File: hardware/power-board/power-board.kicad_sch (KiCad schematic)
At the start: 18 parts, among them J1 SW_SPST, J2 Conn_01x04, K1 SPST-NO, K2 SPST-NO, P1 IEC320-C14, P2 IEC320-C13, P3 IEC320-C13, U1 NUD3112DMT1G

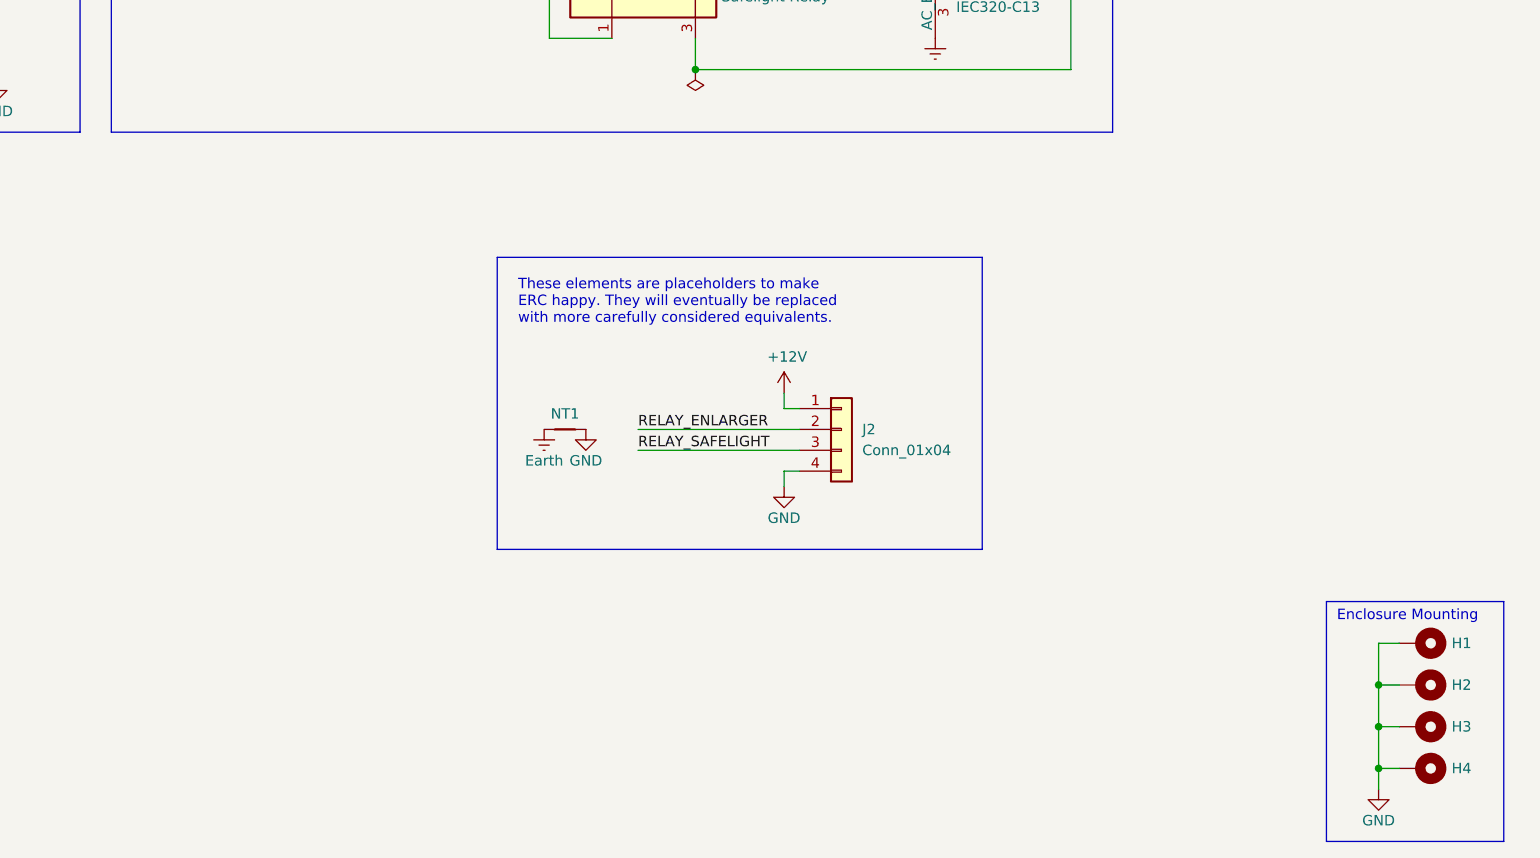
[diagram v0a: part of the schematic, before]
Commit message: WIP of adding XLR5 jack and making mechanical adjustments
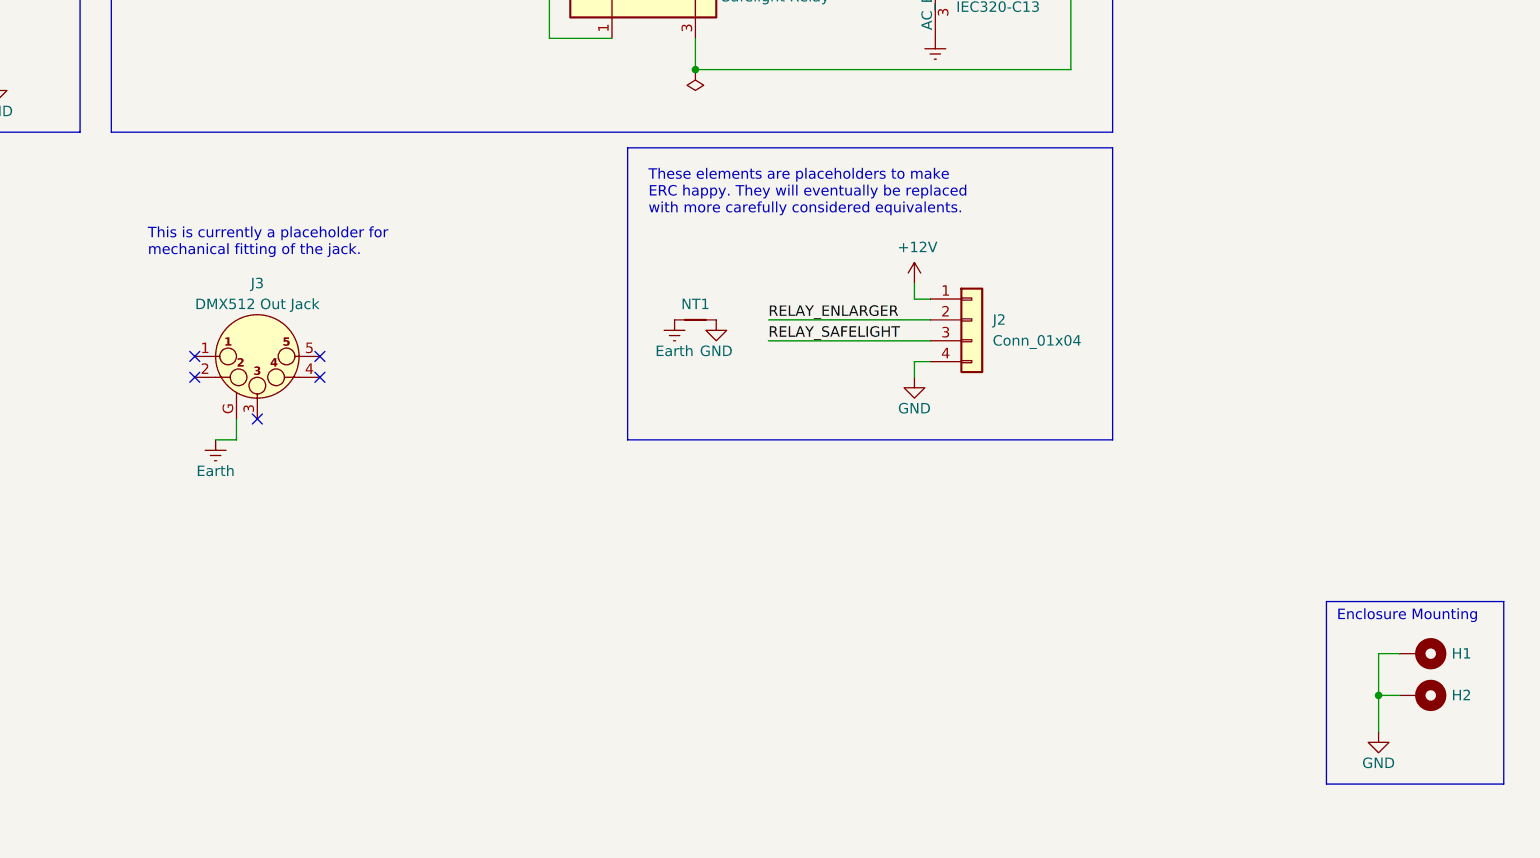
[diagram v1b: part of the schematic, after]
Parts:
- removed H3, H4: MountingHole_Pad, MountingHole:MountingHole_3.2mm_M3_Pad_Via, symbol Mechanical:MountingHole_Pad
- added J3: DMX512 Out Jack, Connector_Audio:Jack_XLR_Neutrik_NC5FBH_Horizontal, symbol Project:XLR5_Ground
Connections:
- net Earth: now also J3.G
- no-connect marks 0 -> 5
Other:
- note added: "This is currently a placeholder for mechanical fitting of the jack."
- moved on the sheet: H1, H2, J2, NT1

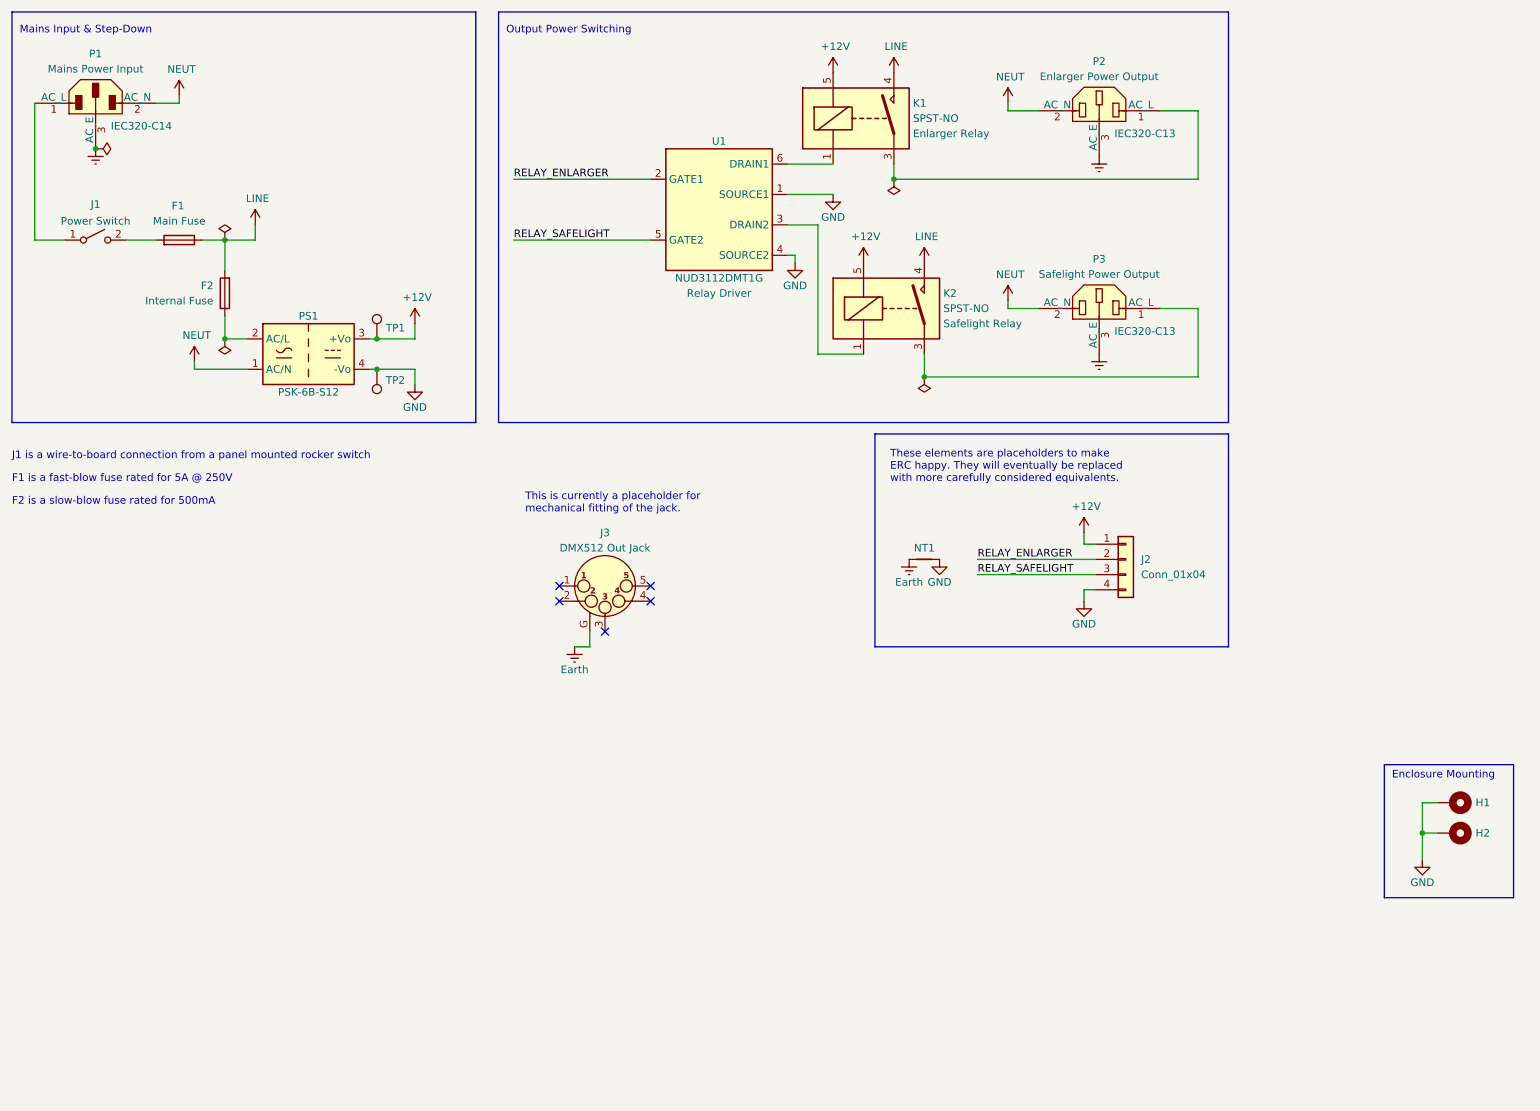
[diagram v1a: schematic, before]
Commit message: Initial addition of RS-485 interface components for DMX512
So far this is just getting the line driver on the board, in addition to
a few support components. Passives and internal connectors are still
placeholders.

The DMX512 spec says the transmitter should be earth referenced, not
isolated, so that helps make our driver and connector decisions.
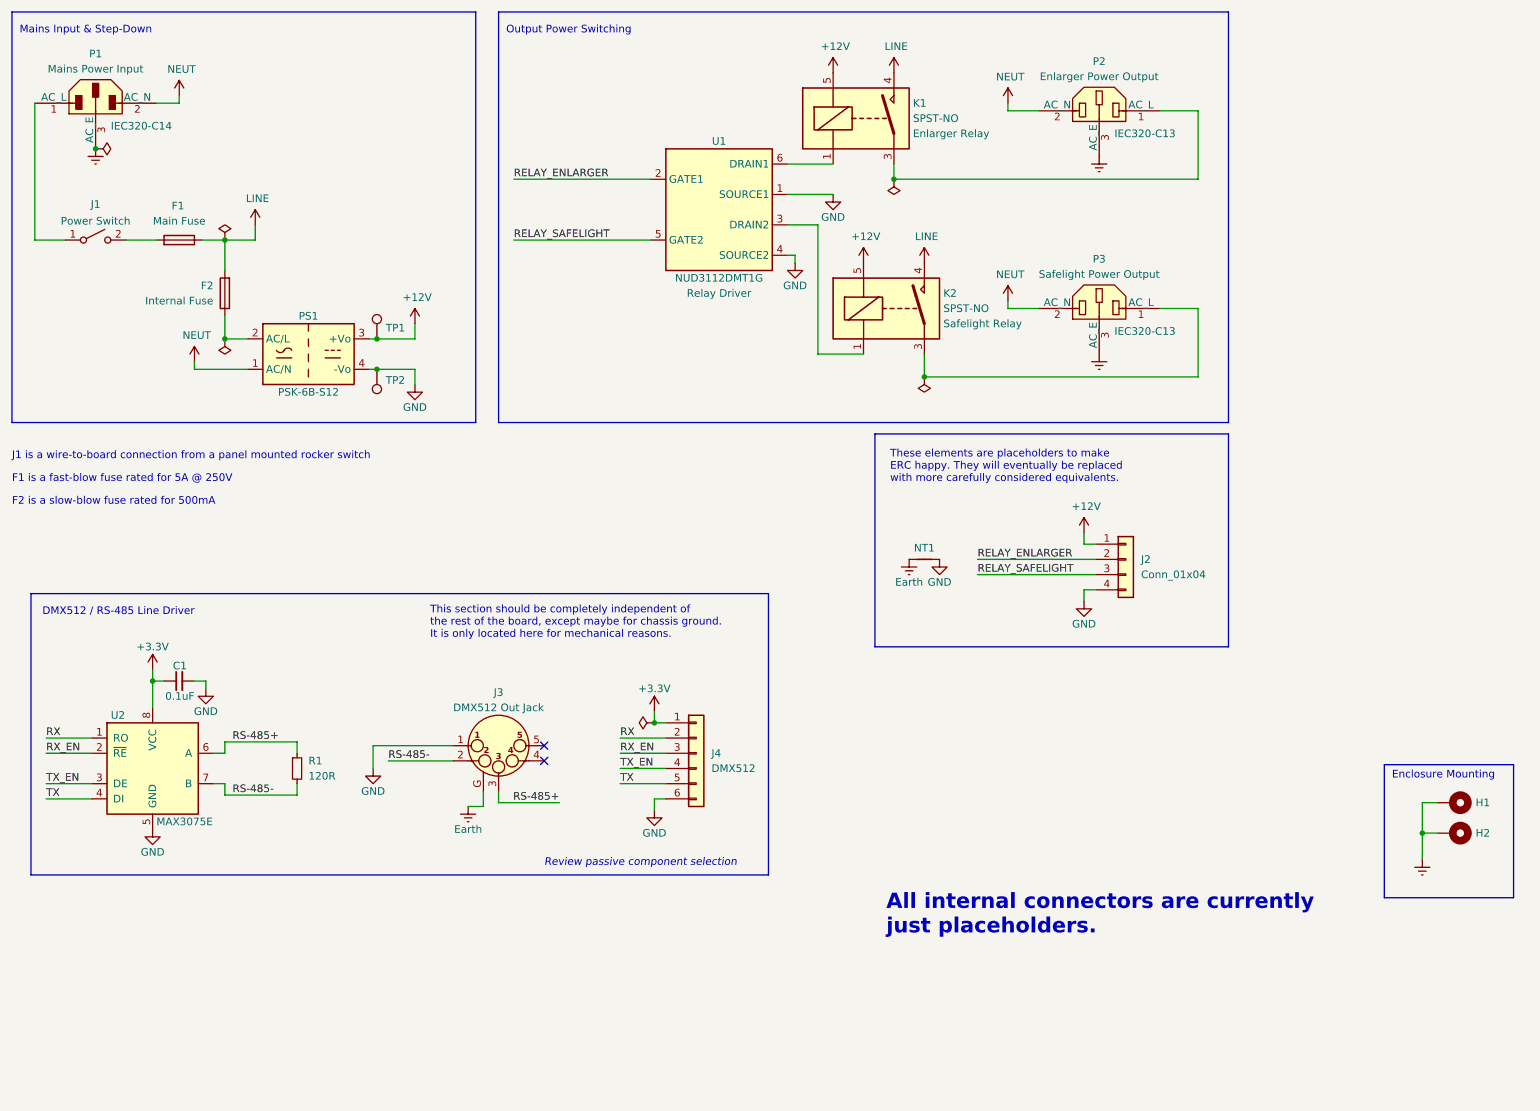
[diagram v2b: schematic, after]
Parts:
- added C1: 0.1uF, Capacitor_SMD:C_0805_2012Metric, symbol Device:C_Small
- added J4: DMX512, Connector_JST:JST_EH_B6B-EH-A_1x06_P2.50mm_Vertical, symbol Connector_Generic:Conn_01x06
- added R1: 120R, Resistor_SMD:R_0805_2012Metric, symbol Device:R_Small
- added U2: MAX3075E, Package_SO:SOIC-8_3.9x4.9mm_P1.27mm, symbol Interface_UART:MAX3075E
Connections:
- net Earth: now also H1.1, H2.1
- net GND: now also J3.1 (P1), C1.2, J4.6 (Pin_6), U2.5 (GND); no longer H1.1, H2.1
- net RS-485-: now reaches J3.2 (P2)
- net RS-485-: now also R1.2, U2.7 (B)
- net RS-485+: now reaches J3.3 (P3)
- net RS-485+: now also R1.1, U2.6 (A)
- new net +3.3V: C1.1, J4.1 (Pin_1), U2.8 (VCC)
- new net RX: J4.2 (Pin_2), U2.1 (RO)
- new net RX_EN: J4.3 (Pin_3), U2.2 (~{RE})
- new net TX: J4.5 (Pin_5), U2.4 (DI)
- new net TX_EN: J4.4 (Pin_4), U2.3 (DE)
- no-connect marks 5 -> 2
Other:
- note added: "All internal connectors are currently just placeholders."
- note added: "DMX512 / RS-485 Line Driver"
- note added: "Review passive component selection"
- note added: "This section should be completely independent of the rest of the board, except maybe for chassis ground. It is only located here for mechanical reasons."
- note removed: "This is currently a placeholder for mechanical fitting of the jack."
- moved on the sheet: J3

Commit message: Initial work on straightening out the AC/DC conversion components
Just some schematic and part selection work for now, to get a few extra
parts in place.
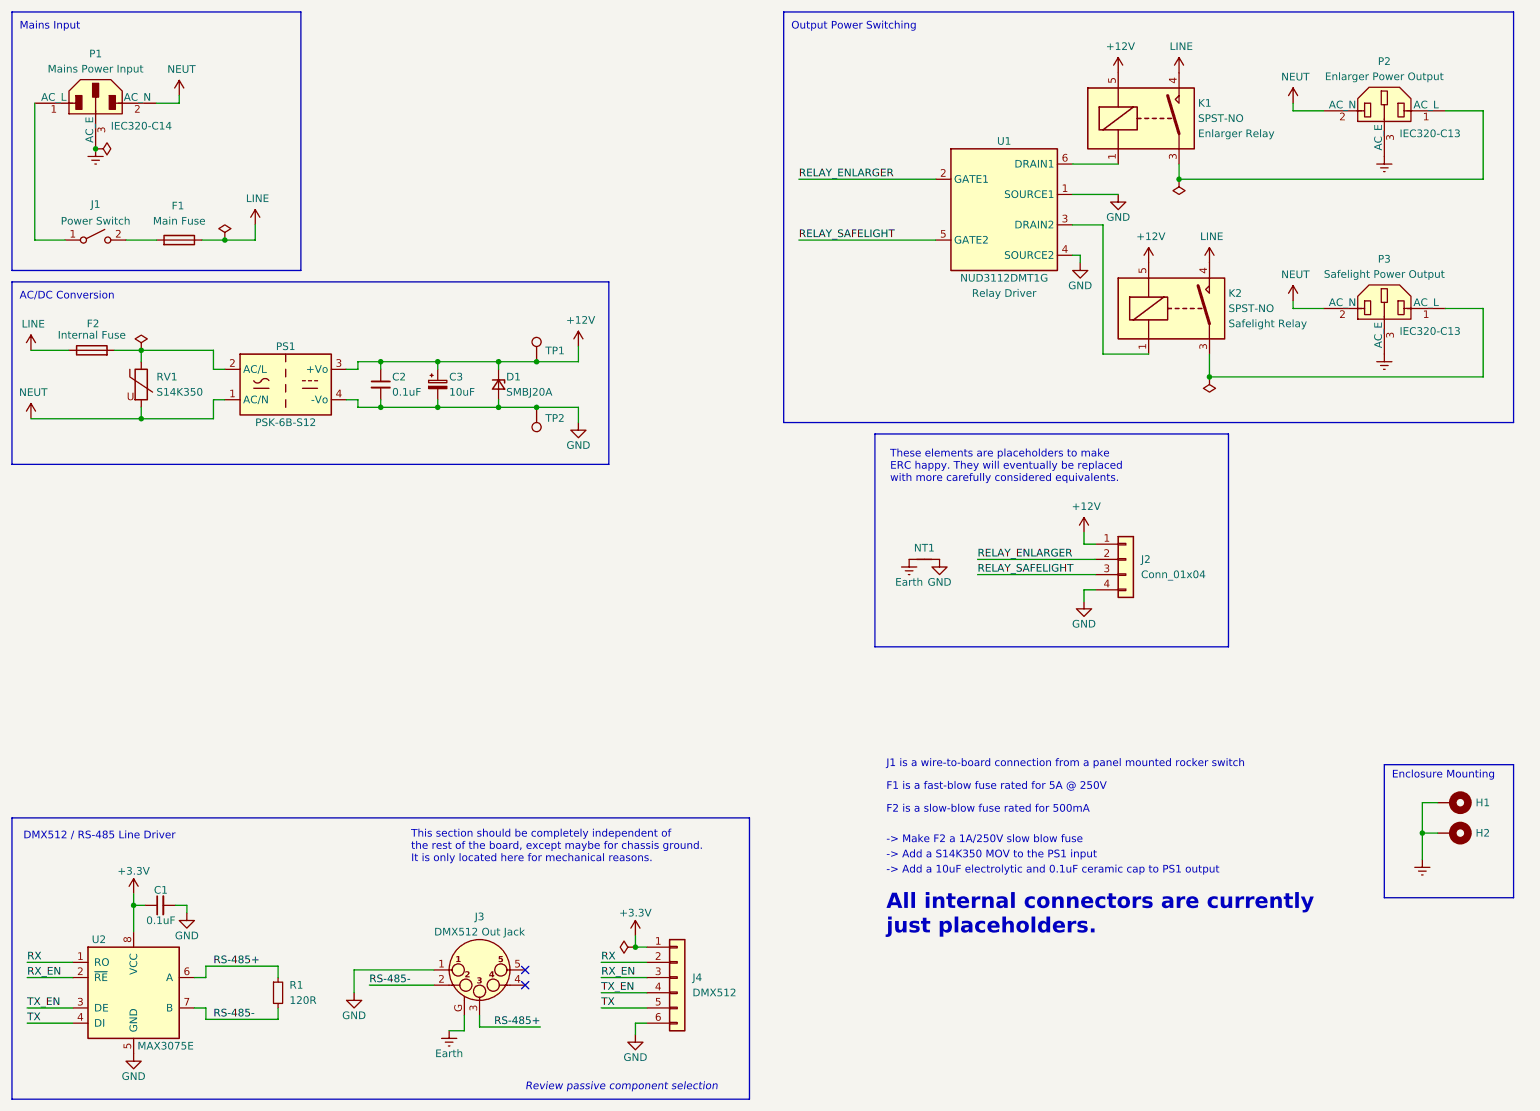
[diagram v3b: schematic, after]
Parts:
- added C2: 0.1uF, Capacitor_SMD:C_1206_3216Metric, symbol Device:C_Small
- added C3: 10uF, Capacitor_SMD:CP_Elec_6.3x5.4, symbol Device:C_Polarized_Small
- added D1: SMBJ20A, Diode_SMD:D_SMB, symbol Device:D_Zener_Small
- added RV1: S14K350, Varistor:RV_Disc_D15.5mm_W5.2mm_P7.5mm, symbol Device:Varistor
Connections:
- net +12V: now also C2.1, C3.1, D1.1 (K)
- net GND: now also C2.2, C3.2, D1.2 (A)
- net LINE: now also F2.1; no longer F2.2
- net NEUT: now also RV1.2
- net at PS1.2 (AC/L): now also F2.2, RV1.1; no longer F2.1
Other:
- note added: "-> Add a 10uF electrolytic and 0.1uF ceramic cap to PS1 output"
- note added: "-> Add a S14K350 MOV to the PS1 input"
- note added: "-> Make F2 a 1A/250V slow blow fuse"
- note added: "AC/DC Conversion"
- note added: "Mains Input"
- note removed: "Mains Input & Step-Down"
- moved on the sheet: C1, F2, J3, J4, K1, K2, P2, P3, PS1, R1, TP1, TP2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

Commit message: Updated MOV footprint
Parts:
- RV1: footprint Varistor:RV_Disc_D15.5mm_W5.2mm_P7.5mm -> lib_fp:RV_Disc_D15.5mm_W5.6mm_P7.5mm
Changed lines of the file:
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@@
       (effects (font (size 1.27 1.27)) (justify left))
     )
-    (property "Footprint" "Varistor:RV_Disc_D15.5mm_W5.2mm_P7.5mm" (id 2) (at 33.782 76.2 90)
+    (property "Footprint" "lib_fp:RV_Disc_D15.5mm_W5.6mm_P7.5mm" (id 2) (at 33.782 76.2 90)
       (effects (font (size 1.27 1.27)) hide)
     )
@@
     )
     (path "/f5398c79-1a1f-4900-9b5f-64ae06197d36"
-      (reference "RV1") (unit 1) (value "S14K350") (footprint "Varistor:RV_Disc_D15.5mm_W5.2mm_P7.5mm")
+      (reference "RV1") (unit 1) (value "S14K350") (footprint "lib_fp:RV_Disc_D15.5mm_W5.6mm_P7.5mm")
     )
     (path "/a48e8f3d-4996-4de2-bb69-8eac29ff1d08"
